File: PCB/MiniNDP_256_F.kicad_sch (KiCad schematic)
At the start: 12 parts, among them J1 Conn_02x20_Odd_Even, U1 HC238, U2 HC4040, U3 HC573, U4 AS6C2008A_DIP32_SOP32

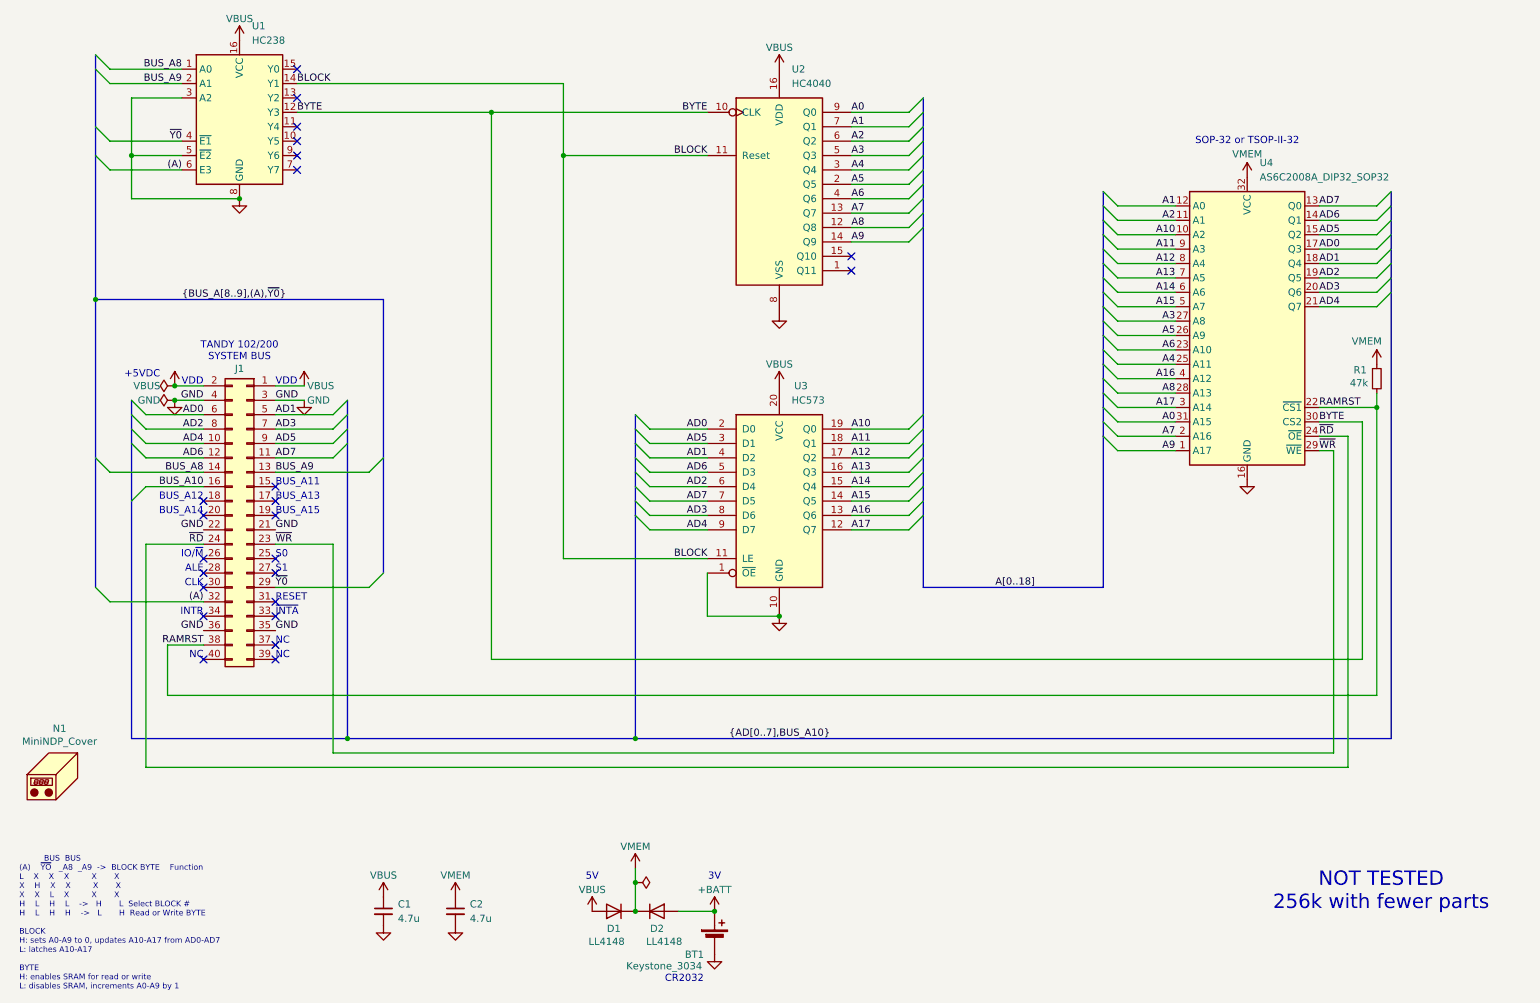
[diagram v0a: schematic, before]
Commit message: easy boards add 47u cap, remove ramrst diode
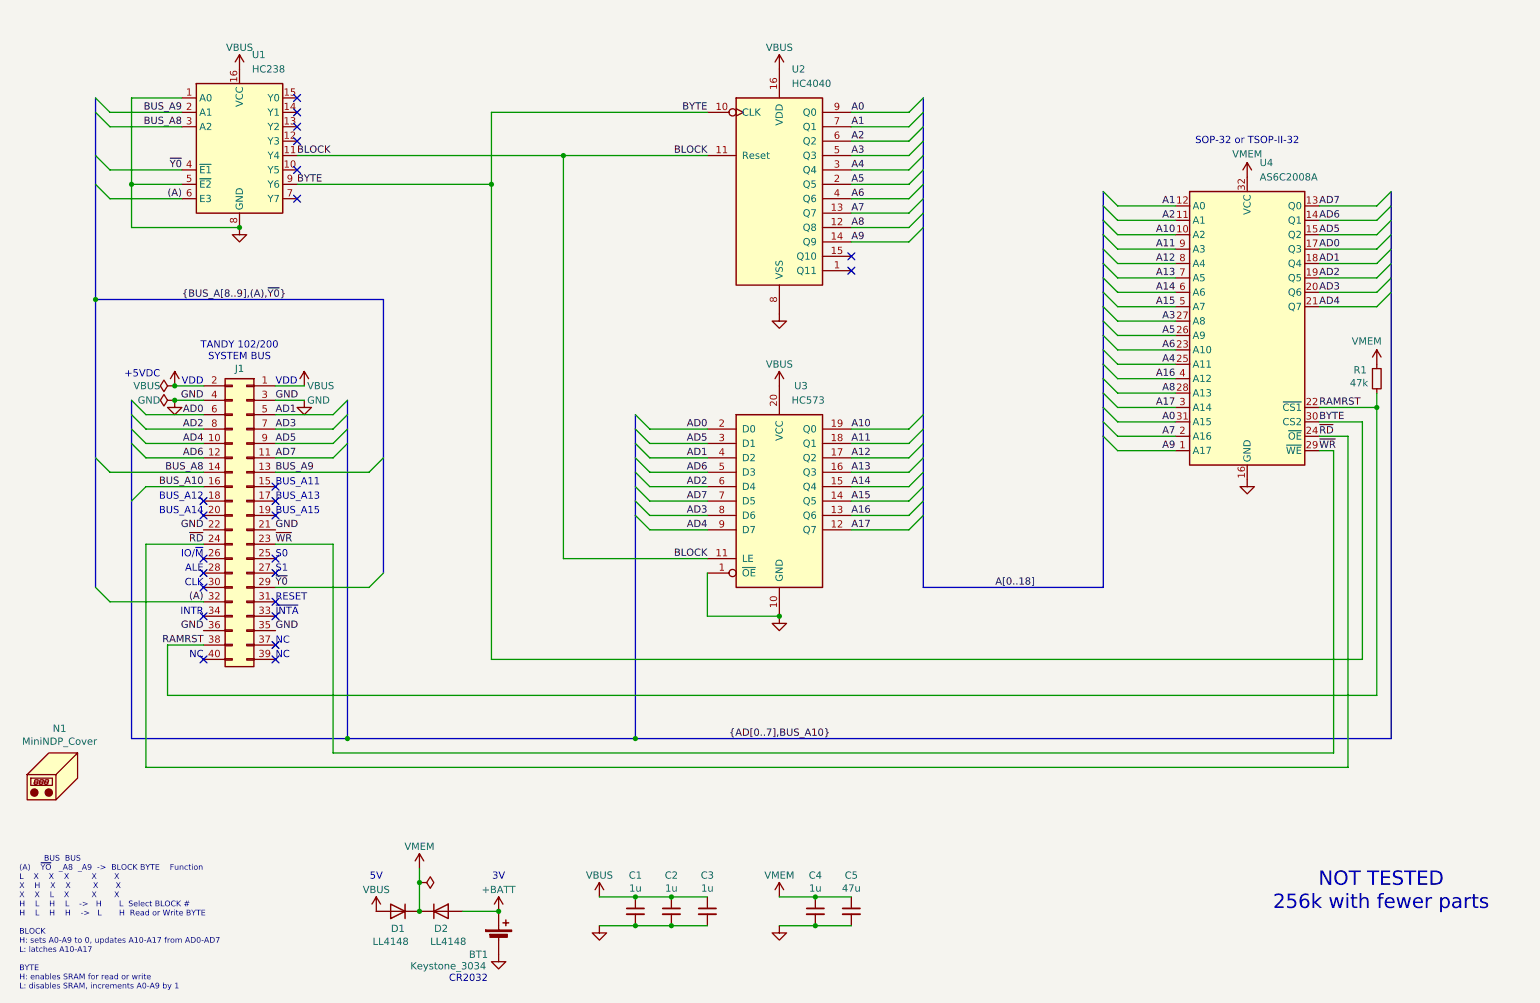
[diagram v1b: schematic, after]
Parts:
- added C3, C4: 1u, 000_LOCAL:C_1206, symbol 000_LOCAL:C
- added C5: 47u, 000_LOCAL:C_1206, symbol 000_LOCAL:C
- C1, C2: value 4.7u -> 1u; MPN CL31B475KAHNNNE -> CL31B105KAHNNNE
- U4: value AS6C2008A_DIP32_SOP32 -> AS6C2008A
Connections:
- net BLOCK: now also U1.11 (Y4); no longer U1.14 (Y1)
- net BUS_A8: now also U1.3 (A2); no longer U1.1 (A0)
- net BYTE: now also U1.9 (Y6); no longer U1.12 (Y3)
- net GND: now also U1.1 (A0), C3.2, C4.2, C5.2; no longer U1.3 (A2)
- net VBUS: now also C2.1, C3.1
- net VMEM: now also C4.1, C5.1; no longer C2.1
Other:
- moved on the sheet: BT1, D1, D2, U1

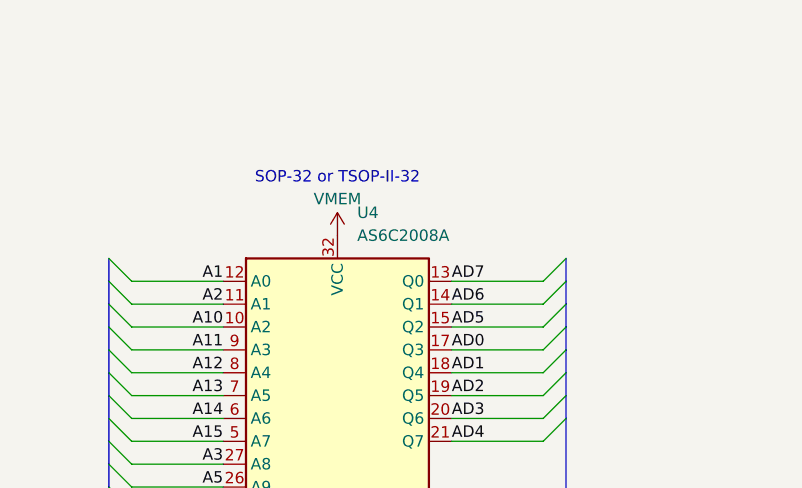
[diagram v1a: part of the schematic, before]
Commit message: alternate 256k sram part
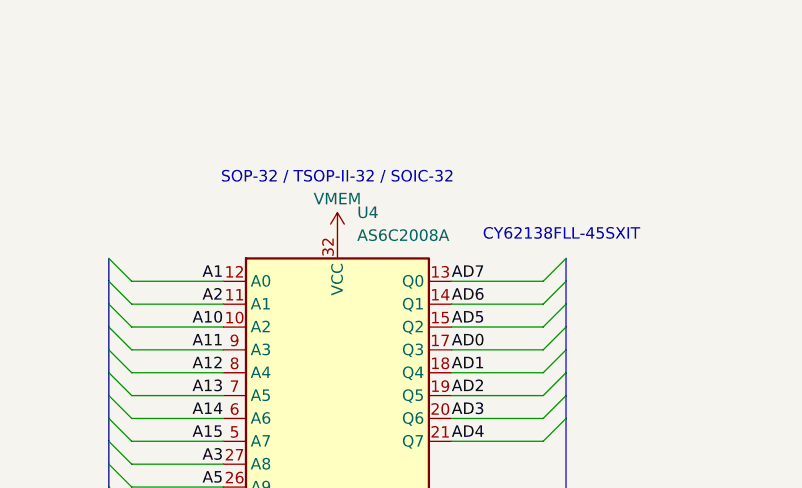
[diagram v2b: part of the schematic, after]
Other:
- note added: "CY62138FLL-45SXIT"
- note added: "SOP-32 / TSOP-II-32 / SOIC-32"
- note removed: "SOP-32 or TSOP-II-32"
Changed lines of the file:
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@@
+		)
+	)
+	(text "CY62138FLL-45SXIT"
+		(exclude_from_sim no)
+		(at 259.842 48.26 0)
+		(effects
+			(font
+				(size 1.27 1.27)
+			)
 		)
 	)
@@
 		)
 	)
-	(text "SOP-32 or TSOP-II-32"
+	(text "SOP-32 / TSOP-II-32 / SOIC-32"
 		(exclude_from_sim no)
 		(at 234.95 41.91 0)
